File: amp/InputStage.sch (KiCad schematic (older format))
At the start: 14 parts

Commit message: reworked amp sheets and notes
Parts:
- added J7: HP_OUT, symbol Connector:AudioJack3
- added J8: MAIN_OUT, symbol Connector:AudioJack3
- added R2, R3, R4: 10K, KiCad/Resistors_ThroughHole.pretty:R_Axial_DIN0204_L3.6mm_D1.6mm_P1.90mm_Vertical, symbol Device:R
- added SW1: SW_DPDT_x2, symbol Switch:SW_DPDT_x2
- added unit 4 of U1
- added unit 4 of U2
- R1: renamed from R?; footprint (none) -> KiCad/Resistors_ThroughHole.pretty:R_Axial_DIN0204_L3.6mm_D1.6mm_P1.90mm_Vertical
- RV1, RV2, RV3, RV4: renamed from RV?; footprint (none) -> KiCad/Resistors_ThroughHole.pretty:R_Axial_DIN0204_L3.6mm_D1.6mm_P1.90mm_Vertical
- U1, U2: renamed from U?; footprint (none) -> KiCad/Housings_DIP.pretty:DIP-14_W7.62mm
- U3: renamed from U?; footprint (none) -> KiCad/Housings_DIP.pretty:DIP-16_W7.62mm
- gave numbers to parts that had none: 6
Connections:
- net labels added: AIN1_DEFAULT, AIN2_DEFAULT, AIN_MIX, AOUT, A_CV_DEFAULT, BIN1_DEFAULT, BIN2_DEFAULT, BIN_MIX, BOUT, B_CV_DEFAULT
- wire segments 82 -> 118
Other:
- note added: "4-osc polyphony requires 4 separate VCAs,\nsince each note needs it’s own envelope.\nTherefore we should switch to 4 single-input VCAs,\ndaisy chained CV, summed with slider for each input.\nNeed to figure out how to set up darlington buffer to\noffer mono-mixdown and stereo from 4 outputs.\nDedicated CV inverter no longer necessary, as this can\nbe handled easily externally (e.g. inverting LFO b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"
- note added: "MIXDOWN"
- note added: "TODO do we need to buffer this?"
- note added: "TODO remaining opamp could be inverter from CVA to CVB\nparams require design since input is not zero-centered"
- note added: "TODO should there even be a HP out? kinda redundant, might conflict if 2\nIn theory, parallel 8ohm loads looks like 4ohm load"
- note added: "TODO: conflicting input impedances"
- note added: "TODO: here we have mixdown before VCA\nso thatdarlington pair can amp the OTA output\nand act as a low output impedance source.\nbut does mixing down first violate the conceptual\nmodel of VCAs A and B?\nWould it work to add the currents together after\nthe darlington buffer and send to both pins?"
- note added: "TODO: should level adjustment be\nat the signal or at the CV?"
- note added: "TODO: should you get access to the mixed signals?\nWhat if you want to apply an effect, e.g. filter, on all inputs?"
- moved on the sheet: R1, RV3, RV4, U1E, U2E, U3E

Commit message: update amp config for quad-cascade design
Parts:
- removed J7: HP_OUT, symbol Connector:AudioJack3
- removed J8: MAIN_OUT, symbol Connector:AudioJack3
- removed R1: 150K, KiCad/Resistors_ThroughHole.pretty:R_Axial_DIN0204_L3.6mm_D1.6mm_P1.90mm_Vertical, symbol Device:R
- removed R2, R3, R4: 10K, KiCad/Resistors_ThroughHole.pretty:R_Axial_DIN0204_L3.6mm_D1.6mm_P1.90mm_Vertical, symbol Device:R
- removed RV1, RV2, RV3, RV4: 100K, KiCad/Resistors_ThroughHole.pretty:R_Axial_DIN0204_L3.6mm_D1.6mm_P1.90mm_Vertical, symbol Device:R_POT
- removed SW1: SW_DPDT_x2, symbol Switch:SW_DPDT_x2
- removed unit 4 of U1
- removed unit 4 of U2
- added J?: CCV_Jack, symbol Connector:AudioJack2_Ground_Switch
- added J?: DCV_Jack, symbol Connector:AudioJack2_Ground_Switch
- added unit 1 of U1
- added unit 1 of U2
- added U3, U4: TL074, symbol Amplifier_Operational:TL074
- added U?: LM13700, KiCad/Housings_DIP.pretty:DIP-16_W7.62mm, symbol Amplifier_Operational:LM13700
- J?: renamed from J4; value BIN2_Jack -> DIN_Jack
- J?: renamed from J3; value BIN1_Jack -> CIN_Jack
- J?: renamed from J2; value AIN4_Jack -> BIN_Jack
- J?: renamed from J1; value AIN4_Jack -> AIN_Jack
- U1, U2: footprint KiCad/Housings_DIP.pretty:DIP-14_W7.62mm -> (none)
- renumbered J5 to J?, J6 to J?, U3 to U?
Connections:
- net labels added: +5V, AIN, AIN_DEFAULT, BIN, BIN_DEFAULT, CIN, CIN_DEFAULT, C_CV, C_CV_DEFAULT, DIN, DIN_DEFAULT, D_CV, D_CV_DEFAULT
- net labels removed: AIN1, AIN1_DEFAULT, AIN2, AIN2_DEFAULT, AIN_MIX, AIN_SUM, AOUT, BIN1, BIN1_DEFAULT, BIN2, BIN2_DEFAULT, BIN_MIX, BIN_SUM, BOUT
- wire segments 118 -> 121
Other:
- note added: "0-10Vpp Signal"
- note added: "0-5V CV"
- note added: "For each subsequent CV, if not supplied,\nuse previous CV"
- note added: "If ACV isn’t supplied,\nDefault CV = 5V"
- note removed: "0-5V Signal"
- note removed: "4-osc polyphony requires 4 separate VCAs,\nsince each note needs it’s own envelope.\nTherefore we should switch to 4 single-input VCAs,\ndaisy chained CV, summed with slider for each input.\nNeed to figure out how to set up darlington buffer to\noffer mono-mixdown and stereo from 4 outputs.\nDedicated CV inverter no longer necessary, as this can\nbe handled easily externally (e.g. inverting LFO b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"
- note removed: "If ACV isn’t supplied,\nDefault CV = 4.8V"
- note removed: "If BCV isn’t supplied, use ACV\nThis means you can either use ACV as master,\nor control individually"
- note removed: "MIXDOWN"
- note removed: "TODO do we need to buffer this?"
- note removed: "TODO remaining opamp could be inverter from CVA to CVB\nparams require design since input is not zero-centered"
- note removed: "TODO should there even be a HP out? kinda redundant, might conflict if 2\nIn theory, parallel 8ohm loads looks like 4ohm load"
- note removed: "TODO: conflicting input impedances"
- note removed: "TODO: here we have mixdown before VCA\nso thatdarlington pair can amp the OTA output\nand act as a low output impedance source.\nbut does mixing down first violate the conceptual\nmodel of VCAs A and B?\nWould it work to add the currents together after\nthe darlington buffer and send to both pins?"
- note removed: "TODO: should level adjustment be\nat the signal or at the CV?"
- note removed: "TODO: should you get access to the mixed signals?\nWhat if you want to apply an effect, e.g. filter, on all inputs?"
- moved on the sheet: J?, U?E

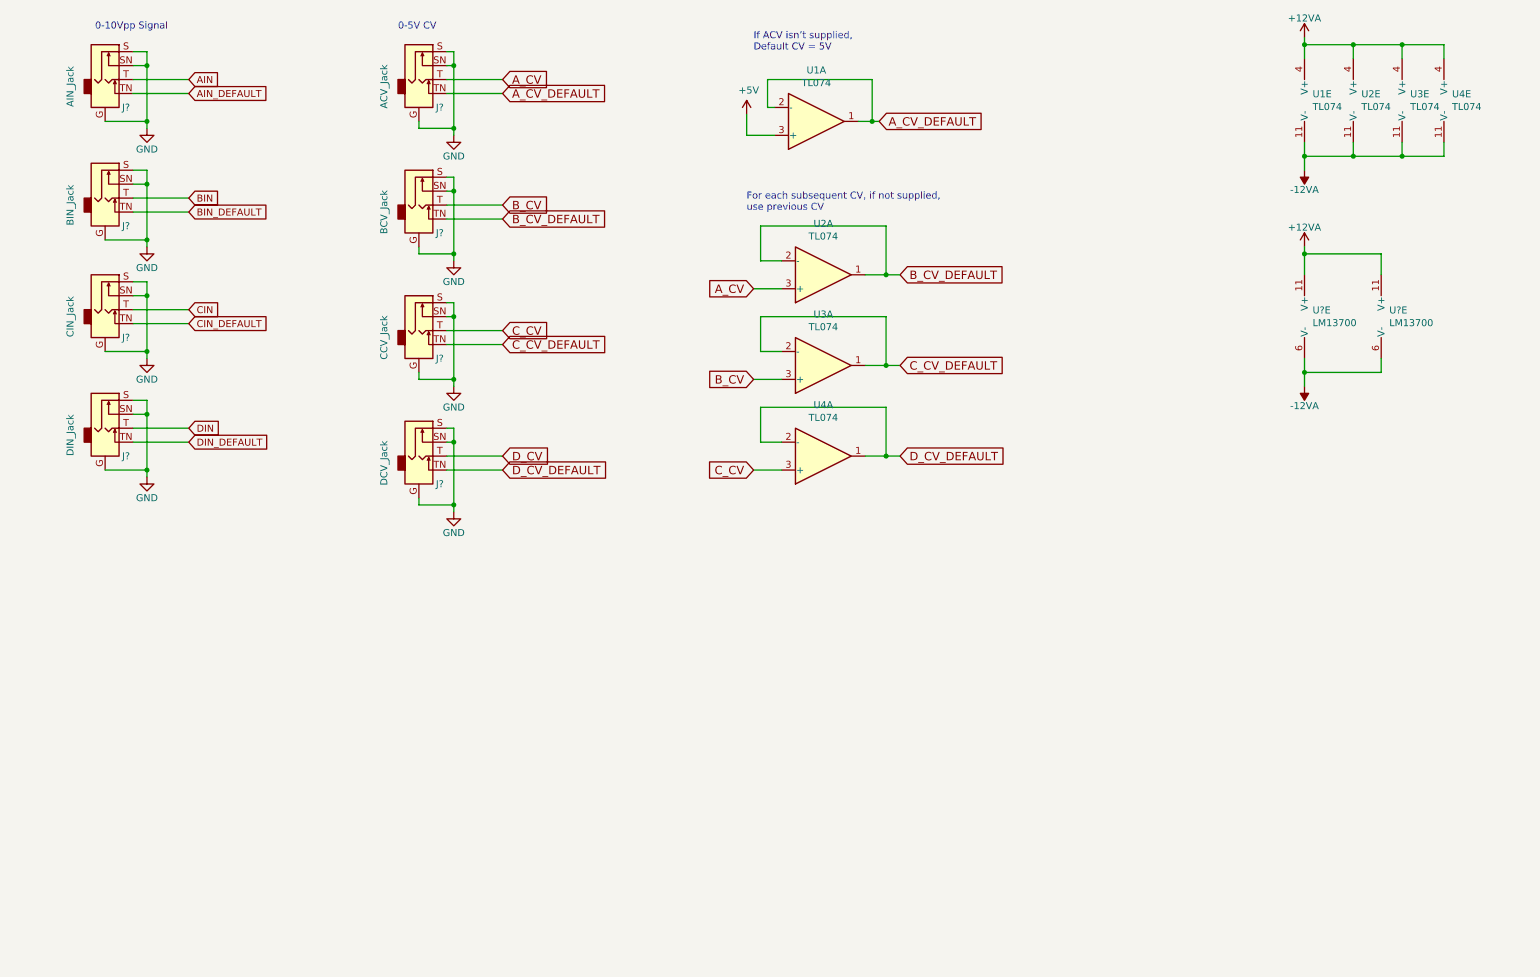
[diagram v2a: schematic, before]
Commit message: add eurorack connector, fix some issues
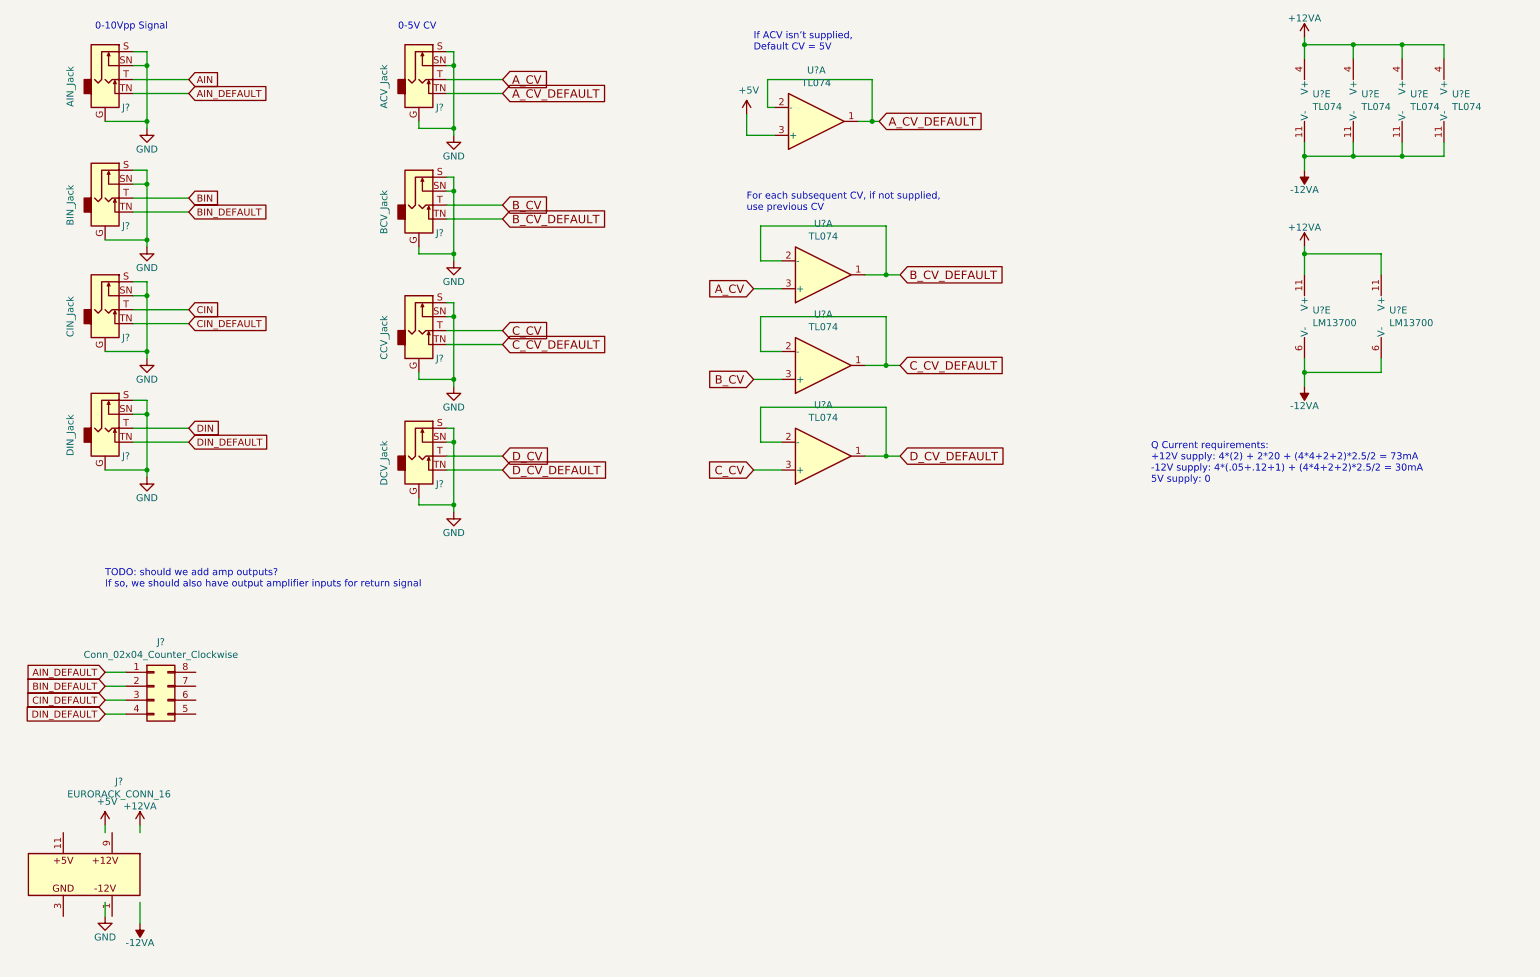
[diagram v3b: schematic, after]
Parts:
- added J?: Conn_02x04_Counter_Clockwise, symbol Connector_Generic:Conn_02x04_Counter_Clockwise
- added J?: EURORACK_CONN_16, KiCad/kicad-footprints/Connector_IDC.pretty:IDC-Header_2x08_P2.54mm_Vertical, symbol synth:EURORACK_CONN_16
- renumbered U1 to U?, U2 to U?, U3 to U?, U4 to U?
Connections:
- wire segments 121 -> 129
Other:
- note added: "Q Current requirements:\n+12V supply: 4*(2) + 2*20 + (4*4+2+2)*2.5/2 = 73mA\n-12V supply: 4*(.05+.12+1) + (4*4+2+2)*2.5/2 = 30mA\n5V supply: 0"
- note added: "TODO: should we add amp outputs?\nIf so, we should also have output amplifier inputs for return signal"
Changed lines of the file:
@@
 $EndComp
 $Comp
-L Amplifier_Operational:TL074 U1
+L Amplifier_Operational:TL074 U?
 U 1 1 5EF7503E
 P 6500 1300
-F 0 "U1" H 6500 933 50  0000 C CNN
+F 0 "U?" H 6500 933 50  0000 C CNN
 F 1 "TL074" H 6500 1024 50  0000 C CNN
 F 2 "" H 6450 1400 50  0001 C CNN
@@
 A_CV
 $Comp
-L Amplifier_Operational:TL074 U1
+L Amplifier_Operational:TL074 U?
 U 5 1 5EFB9B95
 P 10100 1150
-F 0 "U1" H 10058 1196 50  0000 L CNN
+F 0 "U?" H 10058 1196 50  0000 L CNN
 F 1 "TL074" H 10058 1105 50  0000 L CNN
 F 2 "" H 10050 1250 50  0001 C CNN
@@
 	10000 2200 10000 2250
 $Comp
-L Amplifier_Operational:TL074 U2
+L Amplifier_Operational:TL074 U?
 U 1 1 5F0F5B47
 P 6550 2400
-F 0 "U2" H 6550 2033 50  0000 C CNN
+F 0 "U?" H 6550 2033 50  0000 C CNN
 F 1 "TL074" H 6550 2124 50  0000 C CNN
 F 2 "" H 6500 2500 50  0001 C CNN
@@
 $EndComp
 $Comp
-L Amplifier_Operational:TL074 U3
+L Amplifier_Operational:TL074 U?
 U 1 1 5F0F793C
 P 6550 3050
-F 0 "U3" H 6550 2683 50  0000 C CNN
+F 0 "U?" H 6550 2683 50  0000 C CNN
 F 1 "TL074" H 6550 2774 50  0000 C CNN
 F 2 "" H 6500 3150 50  0001 C CNN
@@
 $EndComp
 $Comp
-L Amplifier_Operational:TL074 U4
+L Amplifier_Operational:TL074 U?
 U 1 1 5F0F8F3C
 P 6550 3700
-F 0 "U4" H 6550 3333 50  0000 C CNN
+F 0 "U?" H 6550 3333 50  0000 C CNN
 F 1 "TL074" H 6550 3424 50  0000 C CNN
 F 2 "" H 6500 3800 50  0001 C CNN
@@
 $EndComp
 $Comp
-L Amplifier_Operational:TL074 U2
+L Amplifier_Operational:TL074 U?
 U 5 1 5F0FE5A5
 P 10450 1150
-F 0 "U2" H 10408 1196 50  0000 L CNN
+F 0 "U?" H 10408 1196 50  0000 L CNN
 F 1 "TL074" H 10408 1105 50  0000 L CNN
 F 2 "" H 10400 1250 50  0001 C CNN
@@
 $EndComp
 $Comp
-L Amplifier_Operational:TL074 U3
+L Amplifier_Operational:TL074 U?
 U 5 1 5F0FF34F
 P 10800 1150
-F 0 "U3" H 10758 1196 50  0000 L CNN
+F 0 "U?" H 10758 1196 50  0000 L CNN
 F 1 "TL074" H 10758 1105 50  0000 L CNN
 F 2 "" H 10750 1250 50  0001 C CNN
@@
 $EndComp
 $Comp
-L Amplifier_Operational:TL074 U4
+L Amplifier_Operational:TL074 U?
 U 5 1 5F0FFC0C
 P 11100 1150
-F 0 "U4" H 11058 1196 50  0000 L CNN
+F 0 "U?" H 11058 1196 50  0000 L CNN
 F 1 "TL074" H 11058 1105 50  0000 L CNN
 F 2 "" H 11050 1250 50  0001 C CNN
@@
 Wire Wire Line
 	10000 3100 10000 3000
+Text Notes 8900 3900 0    50   ~ 0
+Q Current requirements:\n+12V supply: 4*(2) + 2*20 + (4*4+2+2)*2.5/2 = 73mA\n-12V supply: 4*(.05+.12+1) + (4*4+2+2)*2.5/2 = 30mA\n5V supply: 0
+Text Notes 1400 4650 0    50   ~ 0
+TODO: should we add amp outputs?\nIf so, we should also have output amplifier inputs for return signal
+$Comp
+L Connector_Generic:Conn_02x04_Counter_Clockwise J?
+U 1 1 5F189CDE
+P 1750 5350
+F 0 "J?" H 1800 5667 50  0000 C CNN
+F 1 "Conn_02x04_Counter_Clockwise" H 1800 5576 50  0000 C CNN
+F 2 "" H 1750 5350 50  0001 C CNN
+F 3 "~" H 1750 5350 50  0001 C CNN
+	1    1750 5350
+	1    0    0    -1
+$EndComp
+Text GLabel 1400 5250 0    50   Input ~ 0
+AIN_DEFAULT
+Text GLabel 1400 5350 0    50   Input ~ 0
+BIN_DEFAULT
+Text GLabel 1400 5450 0    50   Input ~ 0
+CIN_DEFAULT
+Text GLabel 1400 5550 0    50   Input ~ 0
+DIN_DEFAULT
+$Comp
+L synth:EURORACK_CONN_16 J?
+U 1 1 5F1A22AA
+P 1500 6650
+F 0 "J?" H 1500 7267 50  0000 C CNN
+F 1 "EURORACK_CONN_16" H 1500 7176 50  0000 C CNN
+F 2 "KiCad/kicad-footprints/Connector_IDC.pretty:IDC-Header_2x08_P2.54mm_Vertical" H 1550 6650 50  0001 C CNN
+F 3 "https://division-6.com/learn/eurorack-power/" H 1550 6650 50  0001 C CNN
+	1    1500 6650
+	1    0    0    -1
+$EndComp
+$Comp
+L power:+12VA #PWR?
+U 1 1 5F1AC43F
+P 1650 6350
+AR Path="/5F1AC43F" Ref="#PWR?"  Part="1"
+AR Path="/5EB23D44/5F1AC43F" Ref="#PWR?"  Part="1"
+F 0 "#PWR?" H 1650 6200 50  0001 C CNN
+F 1 "+12VA" H 1650 6490 50  0000 C CNN
+F 2 "" H 1650 6350 50  0001 C CNN
+F 3 "" H 1650 6350 50  0001 C CNN
+	1    1650 6350
+	1    0    0    -1
+$EndComp
+$Comp
+L power:-12VA #PWR?
+U 1 1 5F1AD093
+P 1650 7050
+AR Path="/5F1AD093" Ref="#PWR?"  Part="1"
+AR Path="/5EB23D44/5F1AD093" Ref="#PWR?"  Part="1"
+F 0 "#PWR?" H 1650 6900 50  0001 C CNN
+F 1 "-12VA" H 1650 7190 50  0000 C CNN
+F 2 "" H 1650 7050 50  0001 C CNN
+F 3 "" H 1650 7050 50  0001 C CNN
+	1    1650 7050
+	-1   0    0    1
+$EndComp
+$Comp
+L power:GND #PWR?
+U 1 1 5F1AD919
+P 1400 7000
+F 0 "#PWR?" H 1400 6750 50  0001 C CNN
+F 1 "GND" H 1400 6850 50  0000 C CNN
+F 2 "" H 1400 7000 50  0001 C CNN
+F 3 "" H 1400 7000 50  0001 C CNN
+	1    1400 7000
+	1    0    0    -1
+$EndComp
+$Comp
+L power:+5V #PWR?
+U 1 1 5F1B98F3
+P 1400 6350
+F 0 "#PWR?" H 1400 6200 50  0001 C CNN
+F 1 "+5V" H 1415 6523 50  0000 C CNN
+F 2 "" H 1400 6350 50  0001 C CNN
+F 3 "" H 1400 6350 50  0001 C CNN
+	1    1400 6350
+	1    0    0    -1
+$EndComp
+Wire Wire Line
+	1650 6350 1650 6400
+Wire Wire Line
+	1400 6400 1400 6350
+Wire Wire Line
+	1400 7000 1400 6900
+Wire Wire Line
+	1650 7050 1650 6900
+Wire Wire Line
+	1400 5550 1550 5550
+Wire Wire Line
+	1550 5450 1400 5450
+Wire Wire Line
+	1400 5350 1550 5350
+Wire Wire Line
+	1550 5250 1400 5250
 $EndSCHEMATC

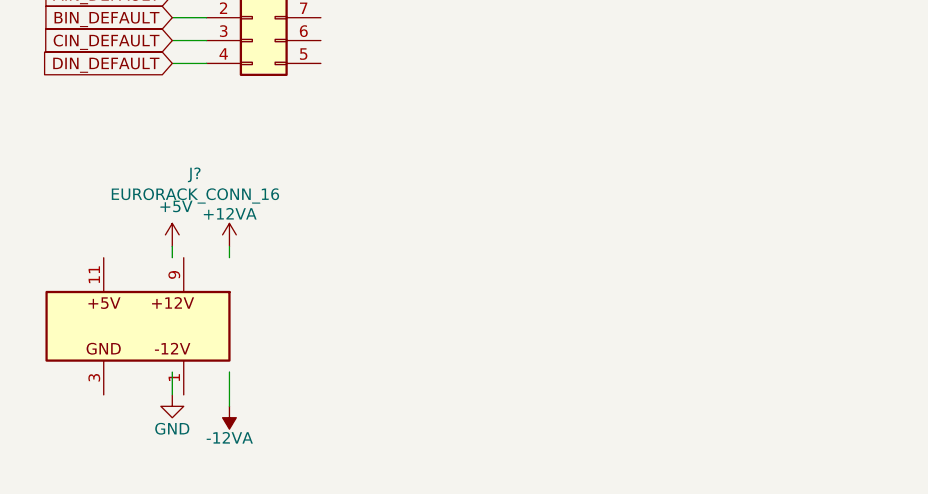
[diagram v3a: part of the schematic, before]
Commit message: added a few more untility footprints
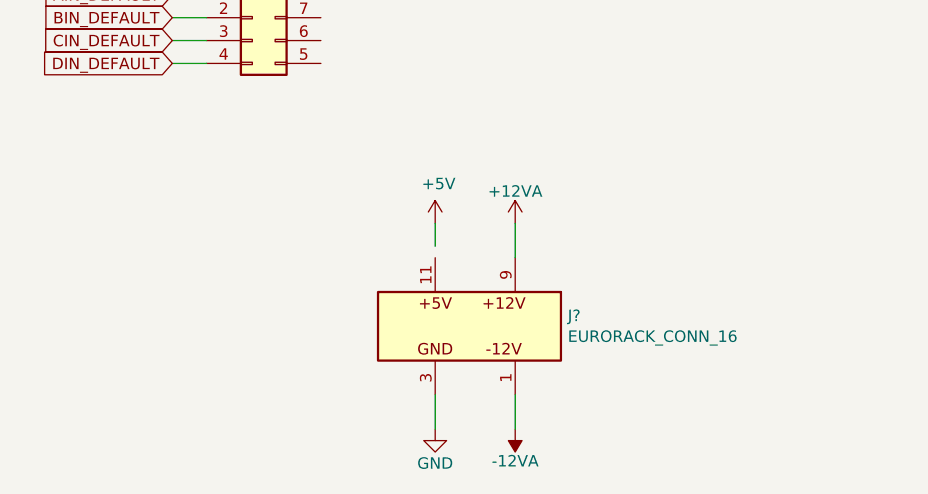
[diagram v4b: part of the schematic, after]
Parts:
- removed J?: EURORACK_CONN_16, KiCad/kicad-footprints/Connector_IDC.pretty:IDC-Header_2x08_P2.54mm_Vertical, symbol synth:EURORACK_CONN_16
- added J?: EURORACK_CONN_16, synth:EURORACK_16_IDC, symbol synth:EURORACK_CONN_16
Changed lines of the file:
@@
 DIN_DEFAULT
-$Comp
-L synth:EURORACK_CONN_16 J?
-U 1 1 5F1A22AA
-P 1500 6650
-F 0 "J?" H 1500 7267 50  0000 C CNN
-F 1 "EURORACK_CONN_16" H 1500 7176 50  0000 C CNN
-F 2 "KiCad/kicad-footprints/Connector_IDC.pretty:IDC-Header_2x08_P2.54mm_Vertical" H 1550 6650 50  0001 C CNN
-F 3 "https://division-6.com/learn/eurorack-power/" H 1550 6650 50  0001 C CNN
-	1    1500 6650
-	1    0    0    -1
-$EndComp
 $Comp
 L power:+12VA #PWR?
 U 1 1 5F1AC43F
-P 1650 6350
+P 2900 6250
 AR Path="/5F1AC43F" Ref="#PWR?"  Part="1"
 AR Path="/5EB23D44/5F1AC43F" Ref="#PWR?"  Part="1"
-F 0 "#PWR?" H 1650 6200 50  0001 C CNN
-F 1 "+12VA" H 1650 6490 50  0000 C CNN
-F 2 "" H 1650 6350 50  0001 C CNN
-F 3 "" H 1650 6350 50  0001 C CNN
-	1    1650 6350
+F 0 "#PWR?" H 2900 6100 50  0001 C CNN
+F 1 "+12VA" H 2900 6390 50  0000 C CNN
+F 2 "" H 2900 6250 50  0001 C CNN
+F 3 "" H 2900 6250 50  0001 C CNN
+	1    2900 6250
 	1    0    0    -1
 $EndComp
@@
 L power:-12VA #PWR?
 U 1 1 5F1AD093
-P 1650 7050
+P 2900 7150
 AR Path="/5F1AD093" Ref="#PWR?"  Part="1"
 AR Path="/5EB23D44/5F1AD093" Ref="#PWR?"  Part="1"
-F 0 "#PWR?" H 1650 6900 50  0001 C CNN
-F 1 "-12VA" H 1650 7190 50  0000 C CNN
-F 2 "" H 1650 7050 50  0001 C CNN
-F 3 "" H 1650 7050 50  0001 C CNN
-	1    1650 7050
+F 0 "#PWR?" H 2900 7000 50  0001 C CNN
+F 1 "-12VA" H 2900 7290 50  0000 C CNN
+F 2 "" H 2900 7150 50  0001 C CNN
+F 3 "" H 2900 7150 50  0001 C CNN
+	1    2900 7150
 	-1   0    0    1
 $EndComp
@@
 L power:GND #PWR?
 U 1 1 5F1AD919
-P 1400 7000
-F 0 "#PWR?" H 1400 6750 50  0001 C CNN
-F 1 "GND" H 1400 6850 50  0000 C CNN
-F 2 "" H 1400 7000 50  0001 C CNN
-F 3 "" H 1400 7000 50  0001 C CNN
-	1    1400 7000
+P 2550 7150
+F 0 "#PWR?" H 2550 6900 50  0001 C CNN
+F 1 "GND" H 2550 7000 50  0000 C CNN
+F 2 "" H 2550 7150 50  0001 C CNN
+F 3 "" H 2550 7150 50  0001 C CNN
+	1    2550 7150
 	1    0    0    -1
 $EndComp
@@
 L power:+5V #PWR?
 U 1 1 5F1B98F3
-P 1400 6350
-F 0 "#PWR?" H 1400 6200 50  0001 C CNN
-F 1 "+5V" H 1415 6523 50  0000 C CNN
-F 2 "" H 1400 6350 50  0001 C CNN
-F 3 "" H 1400 6350 50  0001 C CNN
-	1    1400 6350
+P 2550 6250
+F 0 "#PWR?" H 2550 6100 50  0001 C CNN
+F 1 "+5V" H 2565 6423 50  0000 C CNN
+F 2 "" H 2550 6250 50  0001 C CNN
+F 3 "" H 2550 6250 50  0001 C CNN
+	1    2550 6250
 	1    0    0    -1
 $EndComp
-Wire Wire Line
-	1650 6350 1650 6400
-Wire Wire Line
-	1400 6400 1400 6350
-Wire Wire Line
-	1400 7000 1400 6900
-Wire Wire Line
-	1650 7050 1650 6900
 Wire Wire Line
 	1400 5550 1550 5550
@@
 Wire Wire Line
 	1550 5250 1400 5250
+$Comp
+L synth:EURORACK_CONN_16 J?
+U 1 1 5ECAD463
+P 2950 6650
+F 0 "J?" H 3130 6646 50  0000 L CNN
+F 1 "EURORACK_CONN_16" H 3130 6555 50  0000 L CNN
+F 2 "synth:EURORACK_16_IDC" H 2150 6400 50  0001 C CNN
+F 3 "https://division-6.com/learn/eurorack-power/" V 3000 6700 50  0001 C CNN
+	1    2950 6650
+	1    0    0    -1
+$EndComp
+Wire Wire Line
+	2550 7150 2550 7000
+Wire Wire Line
+	2900 7150 2900 7000
+Wire Wire Line
+	2900 6400 2900 6250
+Wire Wire Line
+	2550 6350 2550 6250
 $EndSCHEMATC
